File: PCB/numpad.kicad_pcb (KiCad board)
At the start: 2 copper layers, 105.6 x 115.1 mm, 65 parts, among them J1 AVR-ISP-6, J2 Conn_01x04_Female, SW1 SW_Push, U1 ProMicro

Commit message: Added mounting holes
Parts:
- added H1: Hole, MountingHole:MountingHole_3.2mm_M3_Pad, F.Cu at (116.7, 170.6)
- added H2: Hole, MountingHole:MountingHole_3.2mm_M3_Pad, F.Cu at (169.9, 134.9)
- added H3: Hole, MountingHole:MountingHole_3.2mm_M3_Pad, F.Cu at (156.4, 99.2)
- added H4: Hole, MountingHole:MountingHole_3.2mm_M3_Pad, F.Cu at (98.4, 98.4)
- MX11, MX15, MX17: footprint CherryMX_KailhSocket_StabWireBottom_LTST-A683CEGBW:CherryMX_2.00u_KailhSocket_StabWireBottom_LTST-A683CEGBW -> CherryMX_PCB_KailhSocket_StabWireBottom_LTST-A683CEGBW:CherryMX_2.00u_PCB_KailhSocket_StabWireBottom_LTST-A683CEGBW
- moved LC7 3.27 mm to (151.6, 92.9), turned to 90 degrees
- moved LC1 2.51 mm to (94.5, 93.7), turned to 90 degrees
- moved ROT1 0.89 mm to (153.6, 72.2)
- moved ROT2 0.40 mm to (177.4, 148.4)
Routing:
- net DOUT1: track 99.6 -> 94.9 mm
- net +5V: track 600.7 -> 596.2 mm
- net ROW1: track 121.3 -> 117.5 mm
- net Net-(MX15-Pad5): track 52.0 -> 54.5 mm
- net COL3: track 146.8 -> 148.1 mm
- net Net-(RD1-Pad2): track 11.2 -> 12.3 mm
- net COL1: track 179.6 -> 178.7 mm
- net ENC_B1: track 28.7 -> 29.3 mm
- net ENC_A1: track 16.1 -> 16.8 mm
- net GND: vias 86 -> 81

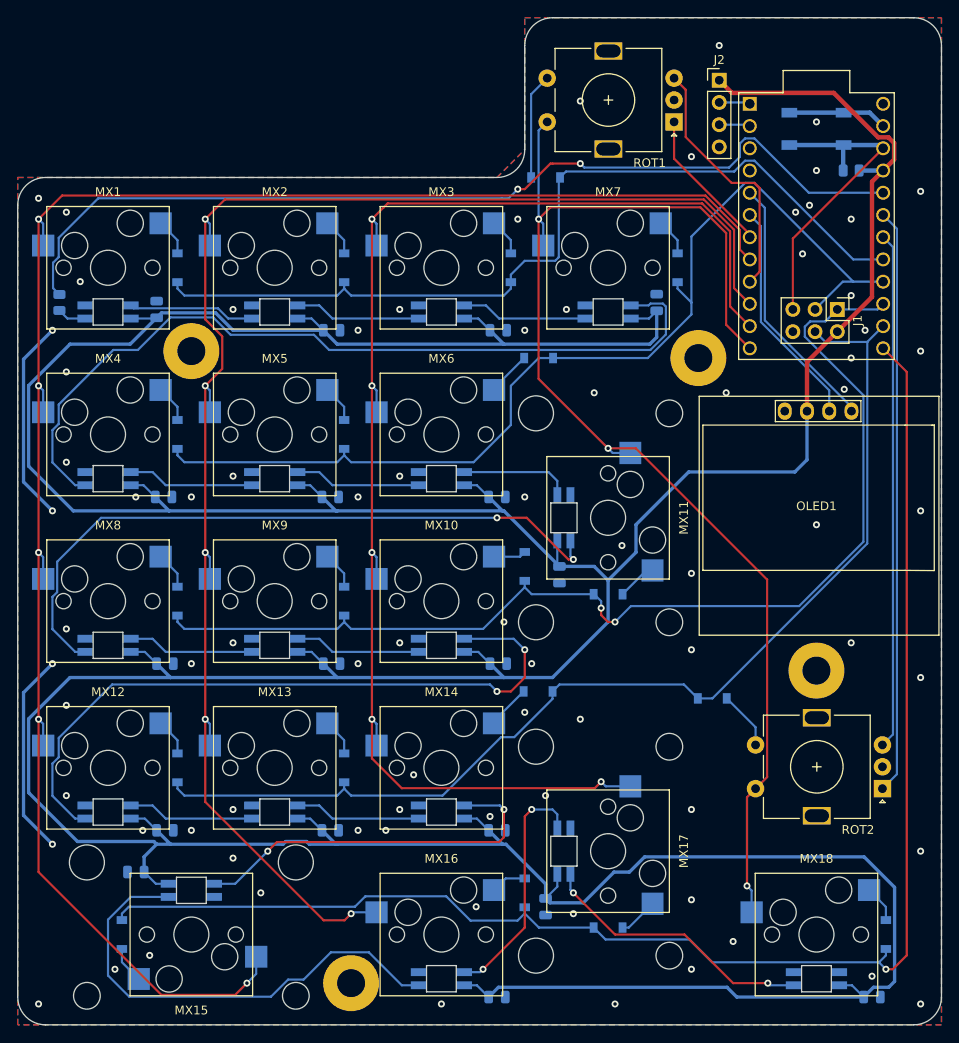
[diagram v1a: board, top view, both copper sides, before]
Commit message: Moved microcontroller by 1/4U
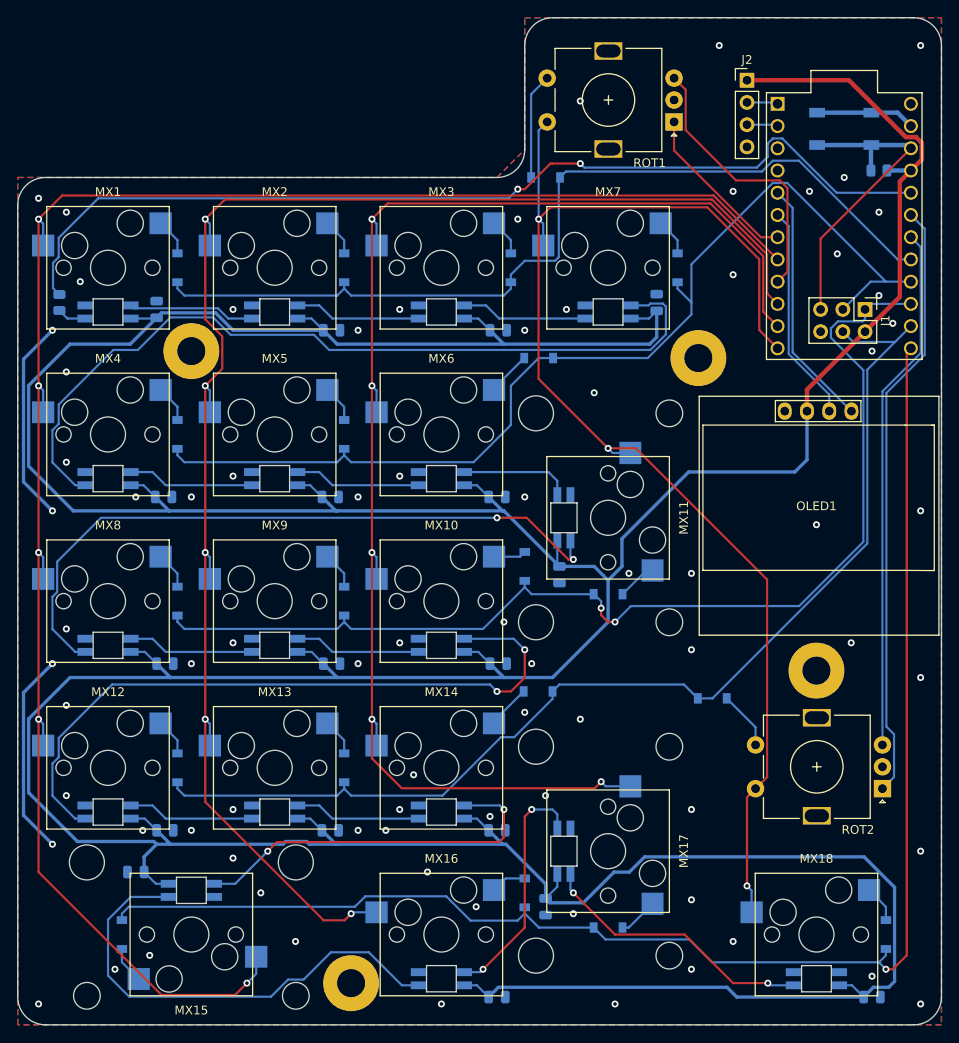
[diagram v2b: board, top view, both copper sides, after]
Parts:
- moved J1 3.17 mm to (175.4, 93.7)
- moved J2 3.17 mm to (161.9, 67.5)
- moved R2 3.17 mm to (177.0, 77.8)
- moved SW1 3.17 mm to (173.0, 73.0)
- moved U1 3.17 mm to (173.0, 84.1)
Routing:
- net ROW0: track 100.3 -> 103.5 mm
- net BKL_DATA_IN: track 109.8 -> 113.0 mm
- net ENC_B1: track 29.3 -> 32.0 mm
- net ENC_A1: track 16.8 -> 19.2 mm
- net ENC_A2: track 66.9 -> 68.9 mm
- net ROW1: track 117.5 -> 119.4 mm
- net COL0: track 207.9 -> 209.8 mm
- net COL1: track 178.7 -> 180.6 mm
- net COL2: track 160.8 -> 162.6 mm
- net COL3: track 148.1 -> 149.8 mm
- net +5V: track 596.2 -> 597.5 mm
- net SDA: track 29.8 -> 28.5 mm
- net SCL: track 26.2 -> 24.9 mm
- net MOSI: track 127.1 -> 128.4 mm
- net ENC_B2: track 59.0 -> 60.3 mm
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
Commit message: Exported gerbers
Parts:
- moved J2 2.51 mm to (159.5, 66.7)
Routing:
- net RX: track 3.56 -> 6.49 mm
- net TX: track 3.56 -> 6.49 mm
- net +5V: track 597.5 -> 600.2 mm
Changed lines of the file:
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@@
     (thickness 1.6)
     (drawings 22)
-    (tracks 665)
+    (tracks 667)
     (zones 0)
     (modules 69)
@@
   )
   (setup
-    (last_trace_width 0.381)
+    (last_trace_width 0.25)
     (user_trace_width 0.2)
     (user_trace_width 0.254)
@@
   )
   (module Connector_PinHeader_2.54mm:PinHeader_1x04_P2.54mm_Vertical (layer F.Cu)
-    (at 161.9148 67.4645)
+    (at 159.5337 66.6708)
     (descr "Through hole straight pin header, 1x04, 2.54mm pitch, single row")
     (tags "Through hole pin header THT 1x04 2.54mm single row")
@@
     (effects (font (size 1 1) (thickness 0.15)) (justify left mirror))
   )
-  (gr_text VCC (at 161.9148 65.0834) (layer B.SilkS)
+  (gr_text VCC (at 159.5337 65.0834) (layer B.SilkS)
     (effects (font (size 1 1) (thickness 0.15)) (justify mirror))
   )
-  (gr_text GND (at 161.9148 77.38575) (layer B.SilkS)
+  (gr_text GND (at 159.5337 76.1952) (layer B.SilkS)
     (effects (font (size 1 1) (thickness 0.15)) (justify mirror))
   )
-  (gr_text RX (at 157.1526 72.62355) (layer B.SilkS)
+  (gr_text RX (at 157.1526 71.82985) (layer B.SilkS)
     (effects (font (size 1 1) (thickness 0.15)) (justify left mirror))
   )
-  (gr_text TX (at 157.1526 70.24245) (layer B.SilkS)
+  (gr_text TX (at 157.1526 69.44875) (layer B.SilkS)
     (effects (font (size 1 1) (thickness 0.15)) (justify left mirror))
   )
@@
   (via (at 155.5652 169.0581) (size 0.8) (drill 0.4) (layers F.Cu B.Cu) (net 3))
   (via (at 80.9574 80.9574) (size 0.8) (drill 0.4) (layers F.Cu B.Cu) (net 3))
-  (via (at 158.74 63.496) (size 0.8) (drill 0.4) (layers F.Cu B.Cu) (net 3))
+  (via (at 158.74 62.7023) (size 0.8) (drill 0.4) (layers F.Cu B.Cu) (net 3))
   (via (at 181.7573 173.0266) (size 0.8) (drill 0.4) (layers F.Cu B.Cu) (net 3))
   (via (at 80.9574 173.0266) (size 0.8) (drill 0.4) (layers F.Cu B.Cu) (net 3))
@@
   (segment (start 151.5967 93.8129) (end 151.5967 96.8314) (width 0.381) (layer B.Cu) (net 5))
   (segment (start 151.5967 96.8314) (end 150.803 97.6251) (width 0.381) (layer B.Cu) (net 5))
-  (segment (start 181.900601 76.528199) (end 180.6466 77.7822) (width 0.508) (layer F.Cu) (net 5))
-  (segment (start 181.900601 74.640279) (end 181.900601 76.528199) (width 0.508) (layer F.Cu) (net 5))
-  (segment (start 181.216523 73.956201) (end 181.900601 74.640279) (width 0.508) (layer F.Cu) (net 5))
-  (segment (start 173.552978 67.4645) (end 180.044679 73.956201) (width 0.508) (layer F.Cu) (net 5))
-  (segment (start 180.044679 73.956201) (end 181.216523 73.956201) (width 0.508) (layer F.Cu) (net 5))
-  (segment (start 161.9148 67.4645) (end 173.552978 67.4645) (width 0.508) (layer F.Cu) (net 5))
   (segment (start 175.4077 96.1966) (end 179.3762 92.2281) (width 0.508) (layer F.Cu) (net 5))
   (segment (start 179.3762 79.0526) (end 180.6466 77.7822) (width 0.508) (layer F.Cu) (net 5))
@@
   (segment (start 147.6282 123.0235) (end 147.6282 119.8487) (width 0.381) (layer B.Cu) (net 5))
   (segment (start 146.0408 124.6109) (end 147.6282 123.0235) (width 0.381) (layer B.Cu) (net 5))
+  (segment (start 181.900601 76.528199) (end 180.6466 77.7822) (width 0.508) (layer F.Cu) (net 5))
+  (segment (start 181.216523 73.956201) (end 181.900601 74.640279) (width 0.508) (layer F.Cu) (net 5))
+  (segment (start 180.044679 73.956201) (end 181.216523 73.956201) (width 0.508) (layer F.Cu) (net 5))
+  (segment (start 181.900601 74.640279) (end 181.900601 76.528199) (width 0.508) (layer F.Cu) (net 5))
+  (segment (start 172.759278 66.6708) (end 180.044679 73.956201) (width 0.508) (layer F.Cu) (net 5))
+  (segment (start 159.5337 66.6708) (end 172.759278 66.6708) (width 0.508) (layer F.Cu) (net 5))
   (via (at 119.055 83.3385) (size 0.8) (drill 0.4) (layers F.Cu B.Cu) (net 6))
   (segment (start 119.582 83.8655) (end 119.055 83.3385) (width 0.25) (layer B.Cu) (net 6))
@@
   (segment (start 170.3277 93.6566) (end 170.3277 85.5611) (width 0.25) (layer F.Cu) (net 16))
   (segment (start 165.2489 72.5445) (end 165.4066 72.7022) (width 0.25) (layer B.Cu) (net 17))
-  (segment (start 161.9148 72.5445) (end 165.2489 72.5445) (width 0.25) (layer B.Cu) (net 17))
+  (segment (start 164.4552 71.7508) (end 165.4066 72.7022) (width 0.25) (layer B.Cu) (net 17))
+  (segment (start 159.5337 71.7508) (end 164.4552 71.7508) (width 0.25) (layer B.Cu) (net 17))
   (segment (start 165.2489 70.0045) (end 165.4066 70.1622) (width 0.25) (layer B.Cu) (net 18))
-  (segment (start 161.9148 70.0045) (end 165.2489 70.0045) (width 0.25) (layer B.Cu) (net 18))
+  (segment (start 164.4552 69.2108) (end 165.4066 70.1622) (width 0.25) (layer B.Cu) (net 18))
+  (segment (start 159.5337 69.2108) (end 164.4552 69.2108) (width 0.25) (layer B.Cu) (net 18))
   (segment (start 91.83161 93.53161) (end 91.4944 93.1944) (width 0.25) (layer B.Cu) (net 19))
   (segment (start 101.46861 93.53161) (end 91.83161 93.53161) (width 0.25) (layer B.Cu) (net 19))
